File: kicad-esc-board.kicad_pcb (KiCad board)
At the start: 2 copper layers, 112 x 34 mm, 7 parts, among them J1 PhoenixContact_01x03_WireToBo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, J2 PhoenixContact_01x02_WireToBo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, J4 JST_01x02_TH_Vertical, M1 Blue Robotics Basic ESC

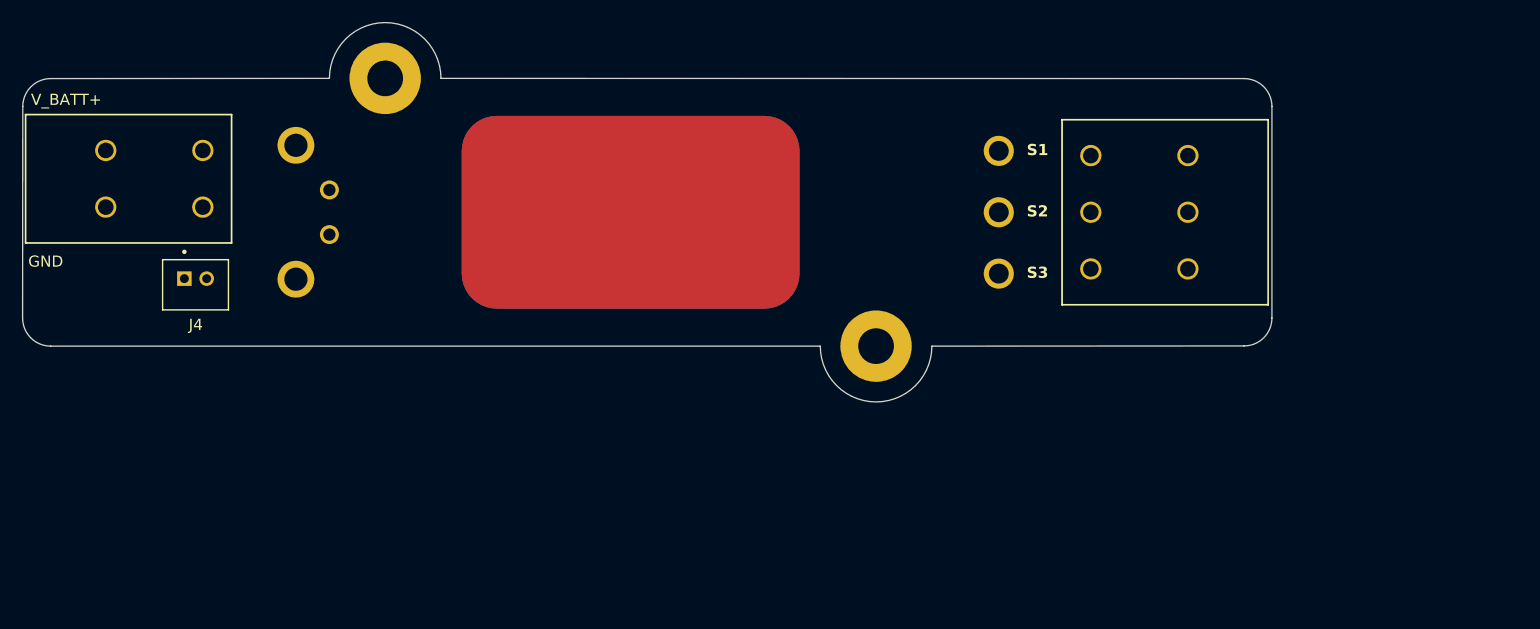
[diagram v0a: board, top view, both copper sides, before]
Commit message: Updated edge cuts and footprints, added .step
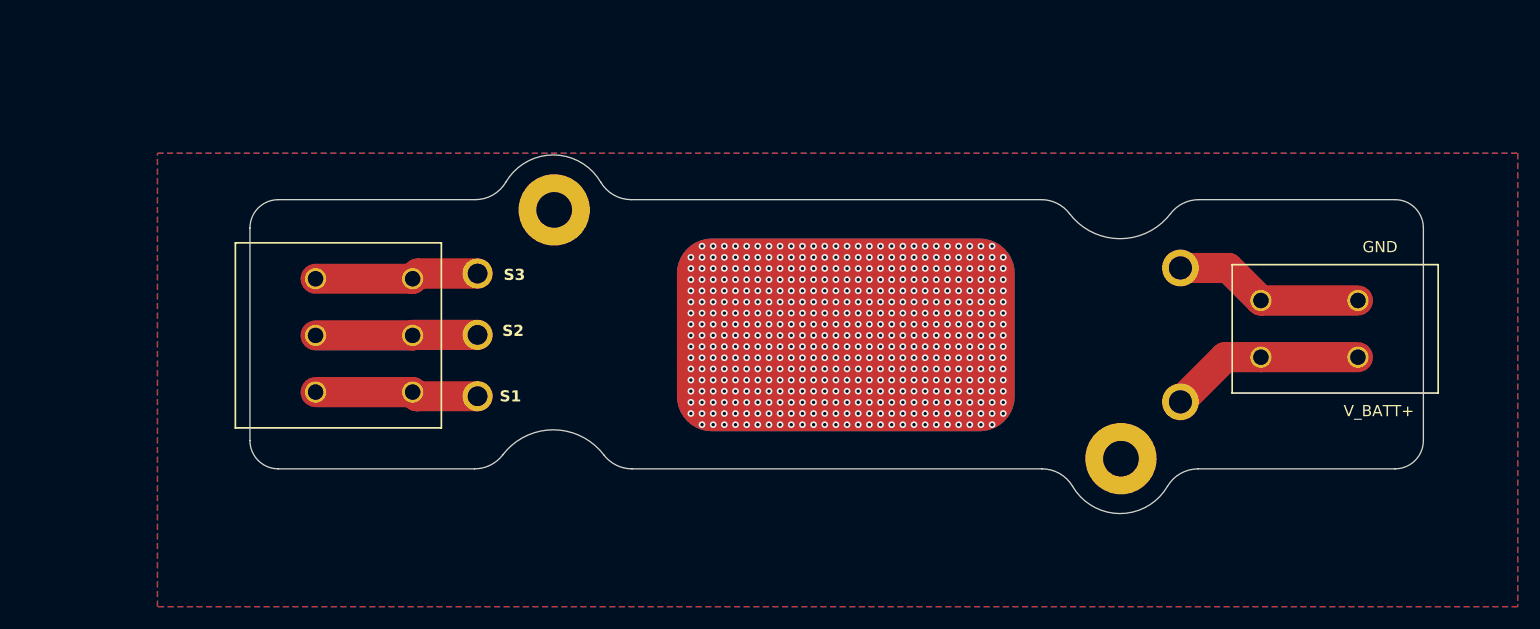
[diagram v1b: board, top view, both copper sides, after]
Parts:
- removed J4: JST_01x02_TH_Vertical, esc_board_custom_footprints:JST_B2B-PH-K-S
- moved J2 112.5 mm to (216.2, 83.4), turned to 90 degrees
- moved J1 81.0 mm to (122.8, 91.6), turned to -90 degrees
- moved HS1 41.7 mm to (170.3, 99.5), turned to 0 degrees
- moved M1 40.8 mm to (169.3, 99.5), turned to 180 degrees
- moved H2 24.2 mm to (194.9, 97.6)
- moved H1 19.2 mm to (144.2, 75.3)
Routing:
- net Net-(J2-Pin_1): track 0.00 -> 17.6 mm
- net GND: track 0.00 -> 17.1 mm, vias 0 -> 489
- net Net-(J1-Pin_3): track 0.00 -> 14.7 mm
- net Net-(J1-Pin_1): track 0.00 -> 14.7 mm
- net Net-(J1-Pin_2): track 0.00 -> 14.5 mm
- added copper zone on B.Cu, net GND
- added copper zone on F.Cu, net GND
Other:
- board size 112 x 34 mm -> 105.2 x 32.1 mm

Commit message: Updated to w/ JST
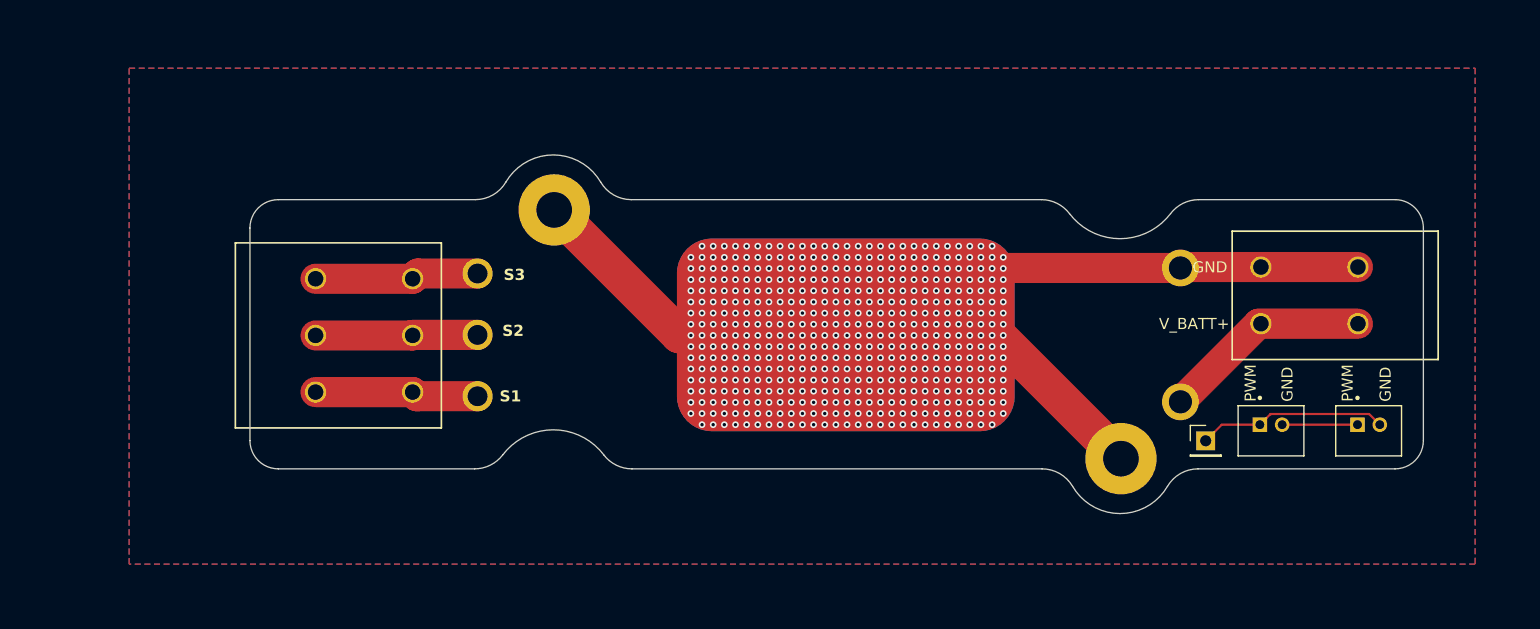
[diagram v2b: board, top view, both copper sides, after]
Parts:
- added J3: Conn_01x01, Connector_PinHeader_2.54mm:PinHeader_1x01_P2.54mm_Vertical, F.Cu at (202.5, 96.0)
- added J4: JST_01x02_TH_Vertical, esc_board_custom_footprints:JST_B2B-PH-K-S, F.Cu at (208.4, 95.1)
- added J5: JST_01x02_TH_Vertical, esc_board_custom_footprints:JST_B2B-PH-K-S, F.Cu at (217.2, 95.1)
- moved J2 3.00 mm to (216.2, 80.4)
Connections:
- J1 pad e: Net-(J1-Pin_3) -> (no net)
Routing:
- net GND: track 17.1 -> 107.3 mm
- net /PWM-Ctrl: track 0.00 -> 17.0 mm
- net /PWM-GND: track 0.00 -> 6.75 mm
- net Net-(J2-Pin_1): track 17.6 -> 18.8 mm
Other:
- board text added: "PWM"

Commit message: Fixed thermal pad corner radius
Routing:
- net GND: vias 489 -> 493
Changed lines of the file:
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@@
 		(sheetname "/")
 		(sheetfile "kicad-esc-board.kicad_sch")
-		(units
-			(unit
-				(name "A")
-				(pins "1" "2" "8" "3" "4" "5")
-			)
-		)
 		(attr smd)
 		(duplicate_pad_numbers_are_jumpers no)
@@
 			(size 30.27 17.27)
 			(layers "F.Cu" "F.Mask" "F.Paste")
-			(roundrect_rratio 0.1815286624)
+			(roundrect_rratio 0.08685581934)
 			(net "GND")
 			(pinfunction "HEAT-SINK_8")
@@
 		(sheetname "/")
 		(sheetfile "kicad-esc-board.kicad_sch")
-		(units
-			(unit
-				(name "A")
-				(pins "1")
-			)
-		)
 		(attr smd)
 		(duplicate_pad_numbers_are_jumpers no)
@@
 			(size 30.27 17.27)
 			(layers "B.Cu" "B.Mask" "B.Paste")
-			(roundrect_rratio 0.1815286624)
+			(roundrect_rratio 0.08685581934)
 			(net "GND")
 			(pintype "passive")
@@
 	)
 	(via
+		(at 184.4 94.54)
+		(size 0.6)
+		(drill 0.3)
+		(layers "F.Cu" "B.Cu")
+		(free yes)
+		(net "GND")
+	)
+	(via
 		(at 182.4 85.54)
 		(size 0.6)
@@
 	)
 	(via
+		(at 184.4 78.54)
+		(size 0.6)
+		(drill 0.3)
+		(layers "F.Cu" "B.Cu")
+		(free yes)
+		(net "GND")
+	)
+	(via
 		(at 169.4 89.54)
 		(size 0.6)
@@
 	)
 	(via
+		(at 156.4 94.54)
+		(size 0.6)
+		(drill 0.3)
+		(layers "F.Cu" "B.Cu")
+		(free yes)
+		(net "GND")
+	)
+	(via
 		(at 164.4 82.54)
 		(size 0.6)
@@
 		(size 0.6)
 		(drill 0.3)
+		(layers "F.Cu" "B.Cu")
+		(free yes)
+		(net "GND")
+	)
+	(via
+		(at 156.4 78.54)
+		(size 0.6)
+		(drill 0.3)
